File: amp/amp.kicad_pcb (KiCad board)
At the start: 2 copper layers, 406.4 x 279.4 mm, 70 parts, among them J1 RCA, J2 Conn_01x05, J3 RCA, J4 JPR_2x3, J5 JPR_2x3, SW1 SW_SPST_GND, SW2 SW_SPDT, SW3 SW_SPDT, T1 Transformer_Hammond_272HX, T2 Hammond 1608A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

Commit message: tweaks
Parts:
- moved C4 4.60 mm to (221.0, 218.4)
- moved C5 3.61 mm to (133.3, 236.2)
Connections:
- net Net-(C11-Pad1) renamed /B+PRE_R
- net Net-(C15-Pad1) renamed /B+PP_R
- net Net-(C3-Pad1) renamed /B+PRE_L
- net Net-(C8-Pad1) renamed /B+PP_L

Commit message: draft routing one channel
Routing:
- net Net-(T1-Pad10): track 0.00 -> 437.1 mm, vias 0 -> 2
- net Net-(T1-Pad12): track 0.00 -> 408.0 mm, vias 0 -> 2
- net Earth: track 0.00 -> 321.9 mm
- net Net-(R7-Pad2): track 0.00 -> 131.3 mm
- net Net-(C4-Pad2): track 0.00 -> 127.1 mm
- net Net-(C7-Pad1): track 0.00 -> 101.2 mm, vias 0 -> 1
- net Net-(C5-Pad2): track 0.00 -> 90.3 mm
- net Net-(T2-Pad4): track 0.00 -> 70.9 mm
- net /B+PP_L: track 0.00 -> 65.9 mm
- net Net-(T2-Pad2): track 0.00 -> 55.6 mm
- net Net-(T2-Pad1): track 0.00 -> 53.0 mm
- net Net-(T2-Pad5): track 0.00 -> 52.4 mm
- net Net-(C4-Pad1): track 0.00 -> 49.9 mm
- net Net-(C2-Pad1): track 0.00 -> 46.0 mm
- net /B+PRE_L: track 0.00 -> 43.4 mm
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
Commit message: update notes and schematic
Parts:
- moved JP1 0.10 mm to (39.1, 42.8)
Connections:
- SW1 pad 5: Earth -> unconnected-(SW1-G2-Pad5)
- T1 pad 5: Net-(T1-Pad5) -> unconnected-(T1-SC-Pad5)
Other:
- net class Default removed

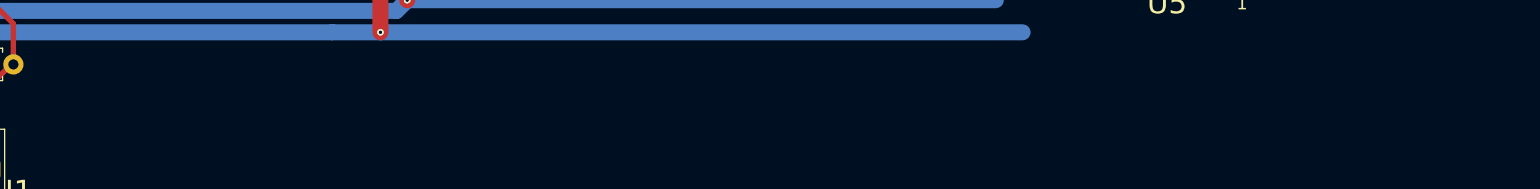
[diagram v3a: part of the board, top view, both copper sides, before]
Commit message: notes and add grid stoppers to schem
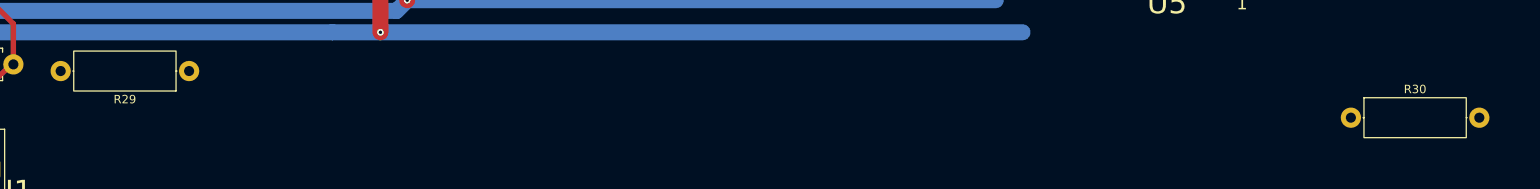
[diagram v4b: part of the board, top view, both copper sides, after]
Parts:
- added R29: 10k, Resistor_THT:R_Axial_DIN0414_L11.9mm_D4.5mm_P15.24mm_Horizontal, F.Cu at (205.3, 262.4)
- added R30: 10k, Resistor_THT:R_Axial_DIN0414_L11.9mm_D4.5mm_P15.24mm_Horizontal, F.Cu at (343.1, 267.9)
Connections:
- U1 pad 1: Net-(J1-In) -> Net-(U1A-G)
- U5 pad 1: Net-(J3-In) -> Net-(U5A-G)
